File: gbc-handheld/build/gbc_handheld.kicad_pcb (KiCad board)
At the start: 2 copper layers, 90 x 98 mm, 23 parts, among them J1 ESP32-S3-DevKitC-1 J1, J3 ESP32-S3-DevKitC-1 J3, SW1 SW_UP, SW2 SW_DOWN, SW3 SW_LEFT, SW4 SW_RIGHT, SW5 SW_A, SW6 SW_B, SW7 SW_START, SW8 SW_SELECT

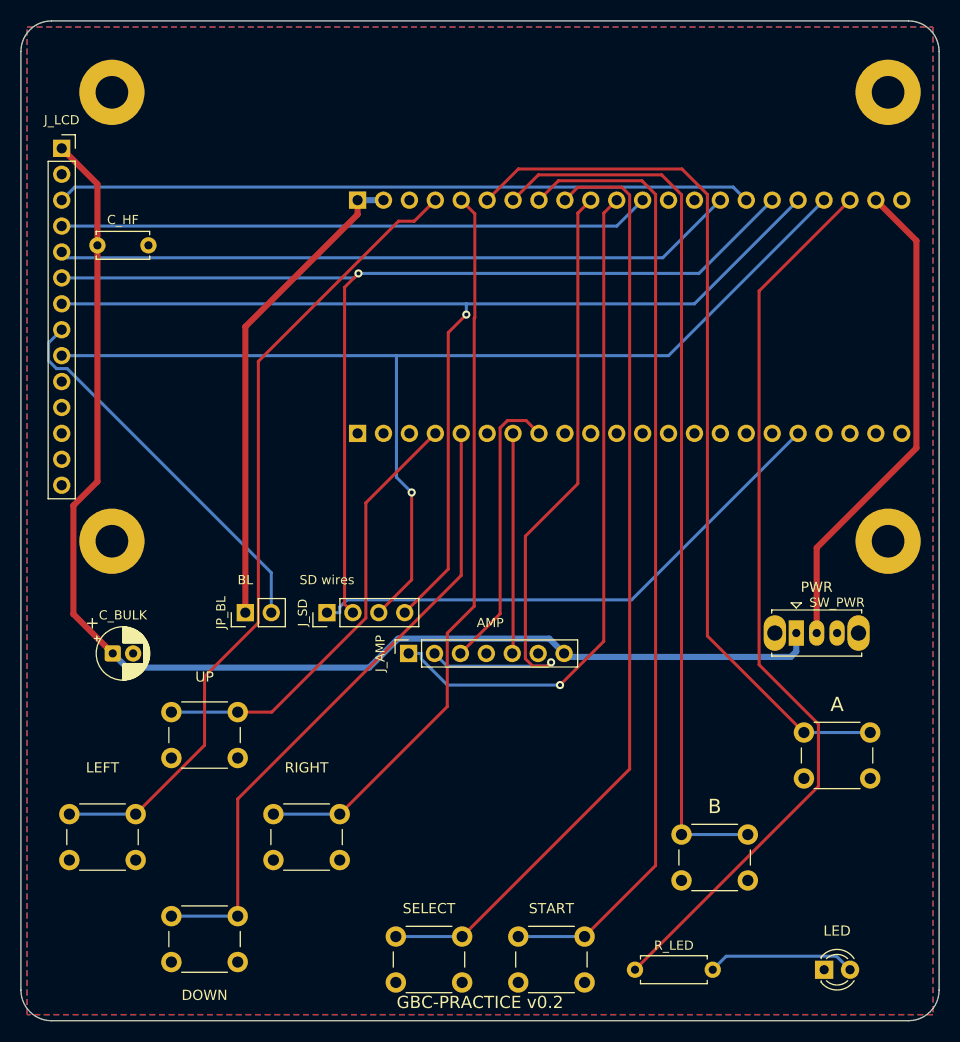
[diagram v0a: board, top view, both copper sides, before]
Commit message: Board v0.3: full audit, 11 fixes, one-command check battery
Audit (spec section 15) found and fixed:
- LCD standoffs must be 11 mm, not 8.5 mm (2.54 mm header spacer)
- slide switch was rated 100 mA but fed the amp: now SS-12D00G3 (0.5 A,
  project footprint) switching only the LCD; amp runs from USB 5 V, muted
  by GPIO; switch position read on GPIO39 via a 15k/22k divider
- LCD MISO left open so it cannot fight the SD card
- backlight from GPIO42 through 1k instead of a jumper
- electrolytic pads 0.40 mm apart -> 2.5 mm pitch footprint (0.9 mm)
- Freerouting's plane assumption left a ground pad floating: ground is now
  routed as tracks and each route is accepted only if KiCad finds 0
  unconnected after the fill
- silkscreen >= 1.0 mm, project rules saved with the board, BOM fixes

New checks (all also shown to fail on deliberately broken input):
check_plugfit.py (Espressif DXF, 44/44 pins), check_3d.py (heights,
standoffs, access paths, pad gaps), check_gerbers.py (drills on copper,
rings, mask), all run by check_all.sh. KiCad DRC: 0 violations.

Co-Authored-By: Claude Opus 5.5 <noreply@anthropic.com>
Claude-Session: https://claude.ai/code/session_018wPBk9DGAqS7vNRLxbgbTv
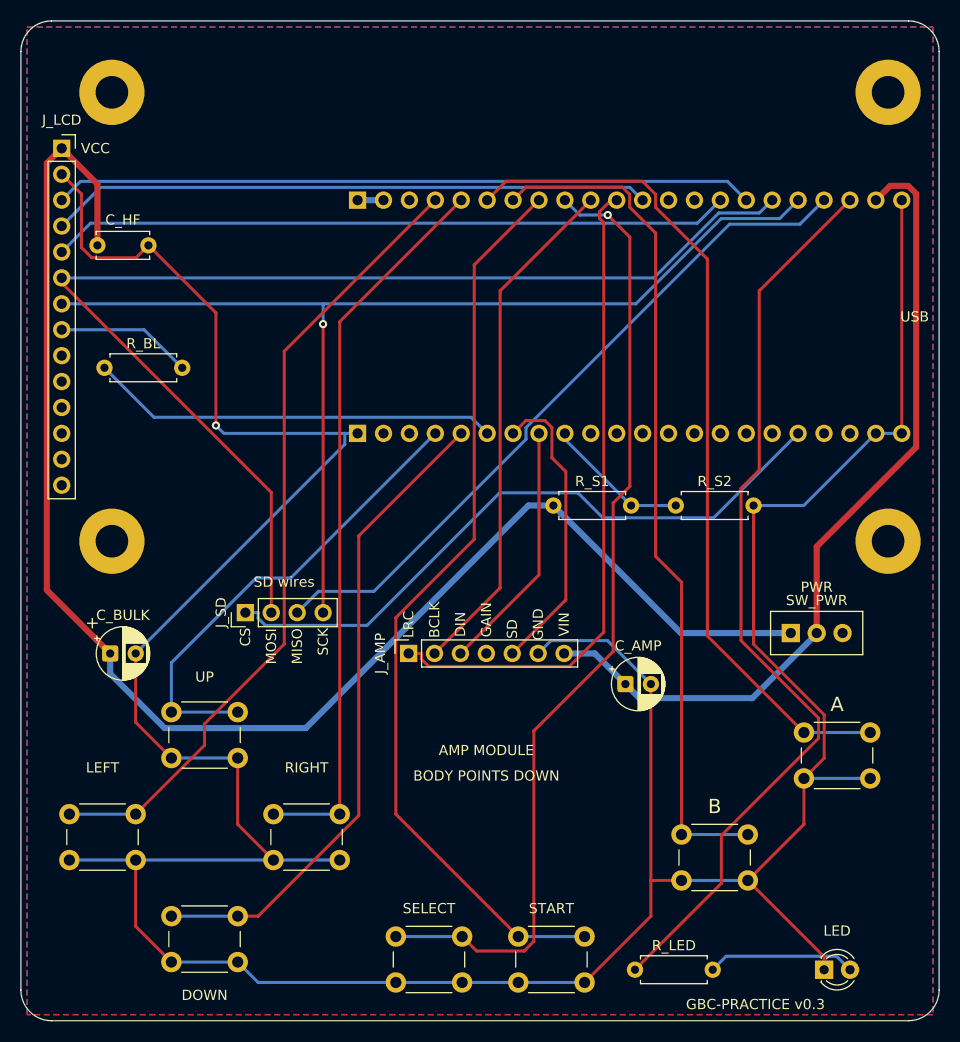
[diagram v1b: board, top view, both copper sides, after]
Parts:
- removed the C_BULK at (69.0, 112.0)
- removed JP_BL: Backlight jumper, Connector_PinHeader_2.54mm:PinHeader_1x02_P2.54mm_Vertical
- removed the SW_PWR at (136.0, 110.0)
- added C_AMP: 100uF, Capacitor_THT:CP_Radial_D5.0mm_P2.50mm, F.Cu at (119.2, 115.0)
- added C_BULK: 100uF, Capacitor_THT:CP_Radial_D5.0mm_P2.50mm, F.Cu at (68.8, 112.0)
- added R_BL: 1k, Resistor_THT:R_Axial_DIN0207_L6.3mm_D2.5mm_P7.62mm_Horizontal, F.Cu at (68.2, 84.0)
- added R_S1: 15k, Resistor_THT:R_Axial_DIN0207_L6.3mm_D2.5mm_P7.62mm_Horizontal, F.Cu at (112.2, 97.5)
- added R_S2: 22k, Resistor_THT:R_Axial_DIN0207_L6.3mm_D2.5mm_P7.62mm_Horizontal, F.Cu at (124.2, 97.5)
- added SW_PWR: Power (slide), gbc:SW_Slide_SS12D00G3, F.Cu at (135.5, 110.0)
- moved J_SD 8.00 mm to (82.0, 108.0)
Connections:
- net LCD_MOSI renamed SPI_MOSI
- net LCD_SCK renamed SPI_SCK
- J1 pad 19: LCD_MISO -> SPI_MISO
- J3 pad 6: (no net) -> LCD_BL
- J3 pad 9: (no net) -> PWR_SENSE
- J_AMP pad 7: +5V_SW -> +5V_USB
- J_LCD pad 9: LCD_MISO -> (no net)
- J_SD pad 3: LCD_MISO -> SPI_MISO
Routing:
- net GND: track 0.00 -> 345.2 mm, vias 0 -> 1
- net LCD_MISO: track 108.2 -> 0.00 mm, vias 1 -> 0
- net SPI_MISO: track 0.00 -> 69.0 mm
- net +3V3: track 47.5 -> 2.54 mm
- net LCD_BL: track 0.00 -> 40.2 mm
- net +5V_USB: track 48.1 -> 81.2 mm
- net N$1: track 37.9 -> 13.4 mm
- net +5V_SW: track 125.1 -> 148.8 mm
- net PWR_SENSE: track 0.00 -> 14.1 mm
- net AUDIO_BCLK: track 62.7 -> 50.8 mm, vias 1 -> 0
- net SD_CS: track 53.8 -> 64.8 mm
- net AUDIO_SD: track 21.6 -> 29.5 mm
- net SPI_MOSI: track 106.9 -> 114.1 mm, vias 1 -> 0
- net BTN_START: track 94.9 -> 89.5 mm
- net BTN_A: track 87.0 -> 83.1 mm
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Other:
- board text added: "AMP MODULE"
- board text added: "BCLK"
- board text added: "BODY POINTS DOWN"
- board text added: "CS"
- board text added: "DIN"
- board text added: "ESP32-S3-DevKitC-1 (underside)"
- board text added: "GAIN"
- board text added: "GBC-PRACTICE v0.3"
- board text added: "GND"
- board text added: "LCD MODULE (11 mm above board)"
- board text added: "LRC"
- board text added: "MISO"
- board text added: "MOSI"
- board text added: "SCK"
- board text added: "SD"
- board text added: "SD SLOT (card enters from top edge)"
- board text added: "USB"
- board text added: "VCC"
- board text added: "VIN"
- board text removed: "AMP"
- board text removed: "BL"
- board text removed: "GBC-PRACTICE v0.2"
